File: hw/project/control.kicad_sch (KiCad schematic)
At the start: 46 parts, among them SW1 RESET, SW2 BOOT0, U7 STSPIN32G4, X1 32MHZ 10PF

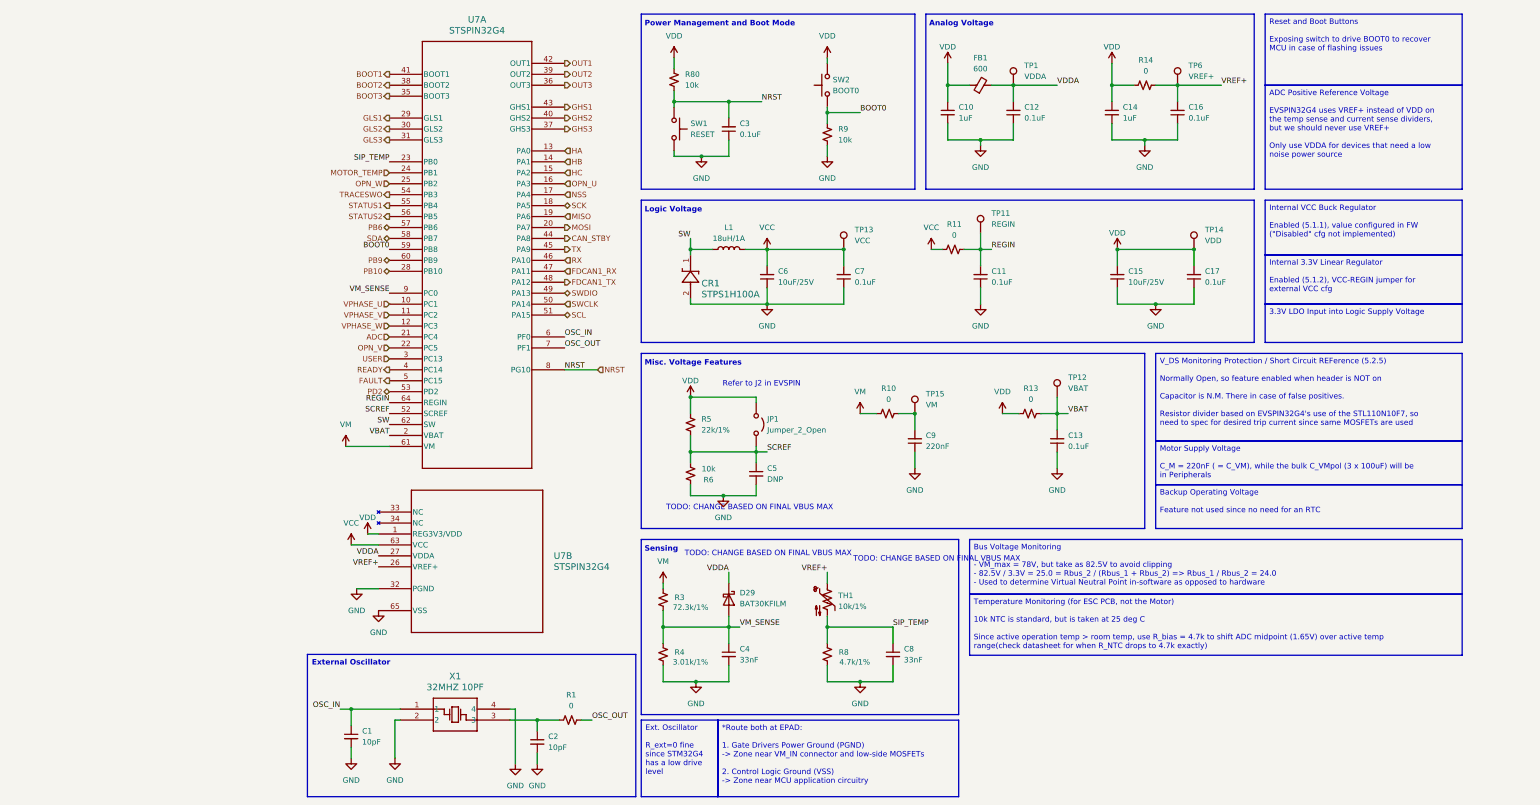
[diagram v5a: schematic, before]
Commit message: Finalize VCC regulator and VDD sections
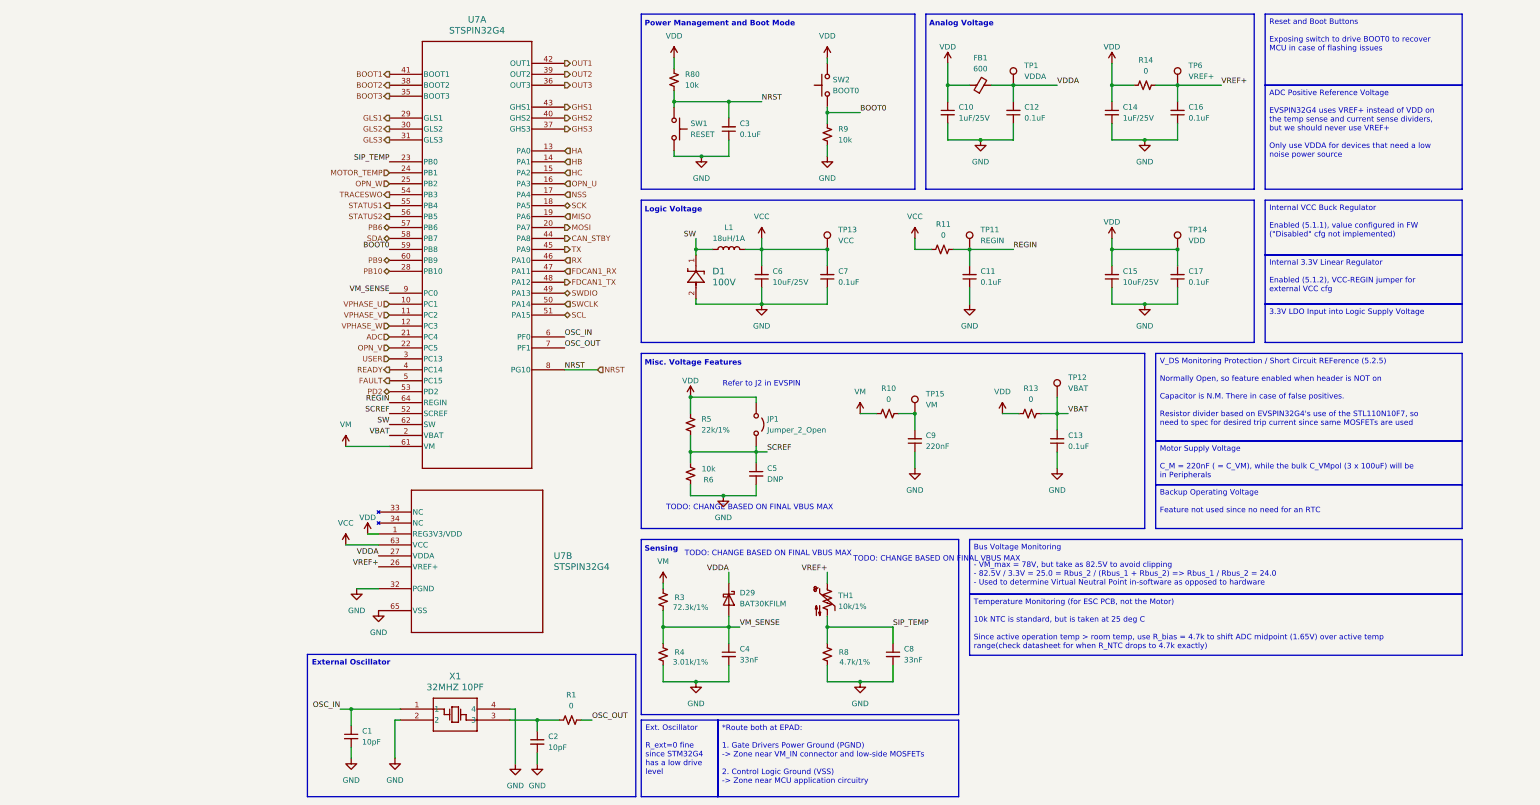
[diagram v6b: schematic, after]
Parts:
- C10, C14: value 1uF -> 1uF/25V
- D1: renamed from CR1; value STPS1H100A -> 100V
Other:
- moved on the sheet: C11, C17, C6, C7, D1, R11, TP11, TP13, TP14

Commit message: Finalize Misc Voltage features
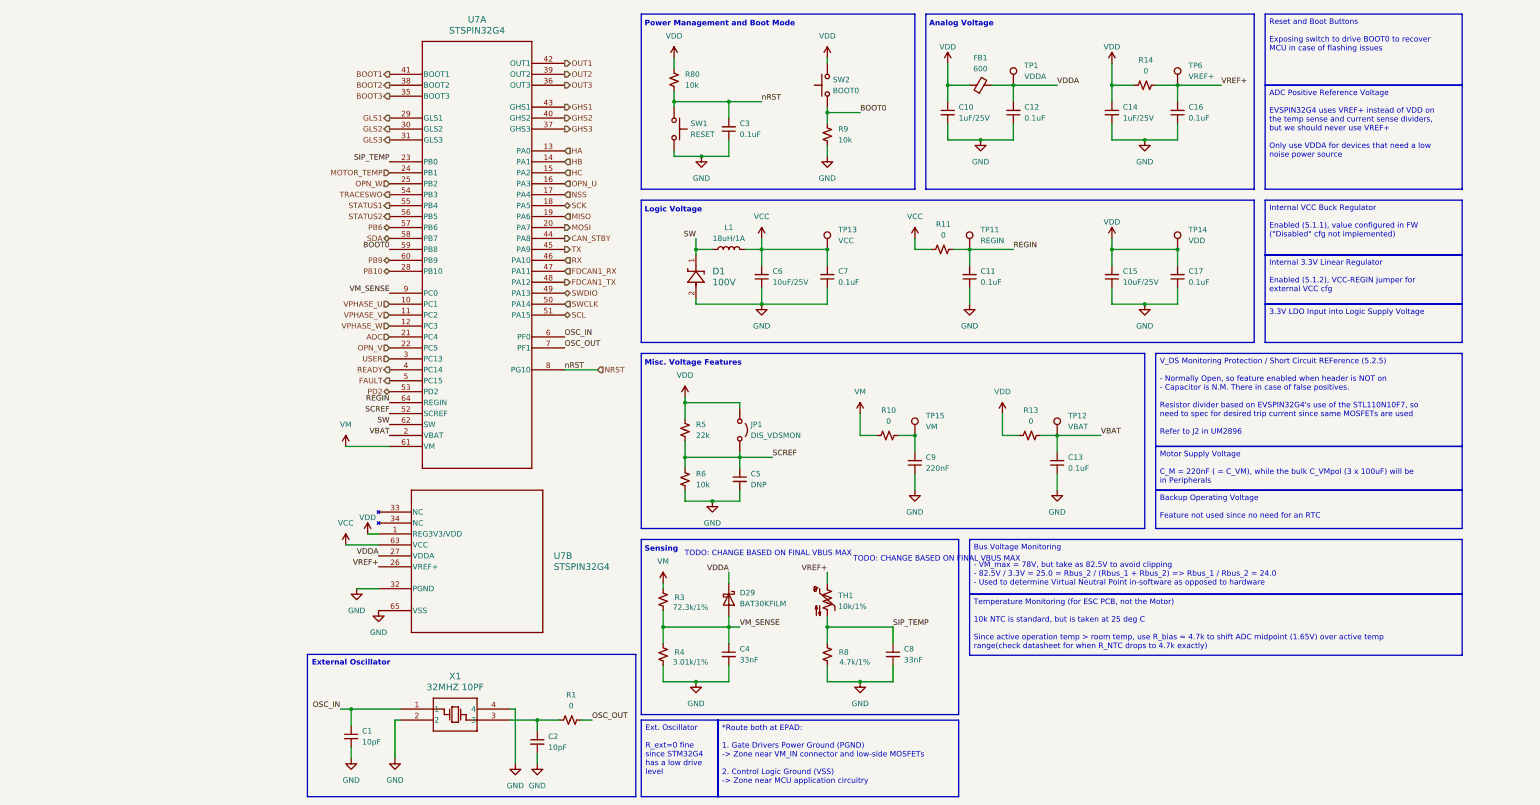
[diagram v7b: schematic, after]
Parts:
- JP1: value Jumper_2_Open -> DIS_VDSMON; footprint (none) -> Connector_PinHeader_2.54mm:PinHeader_1x02_P2.54mm_Vertical
- R5: value 22k/1% -> 22k
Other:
- note removed: "Refer to J2 in EVSPIN"
- moved on the sheet: C13, C5, C9, JP1, R10, R13, R5, R6, TP12, TP15

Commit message: Finished control sheet sensing. Need to work on OSC tomorrow
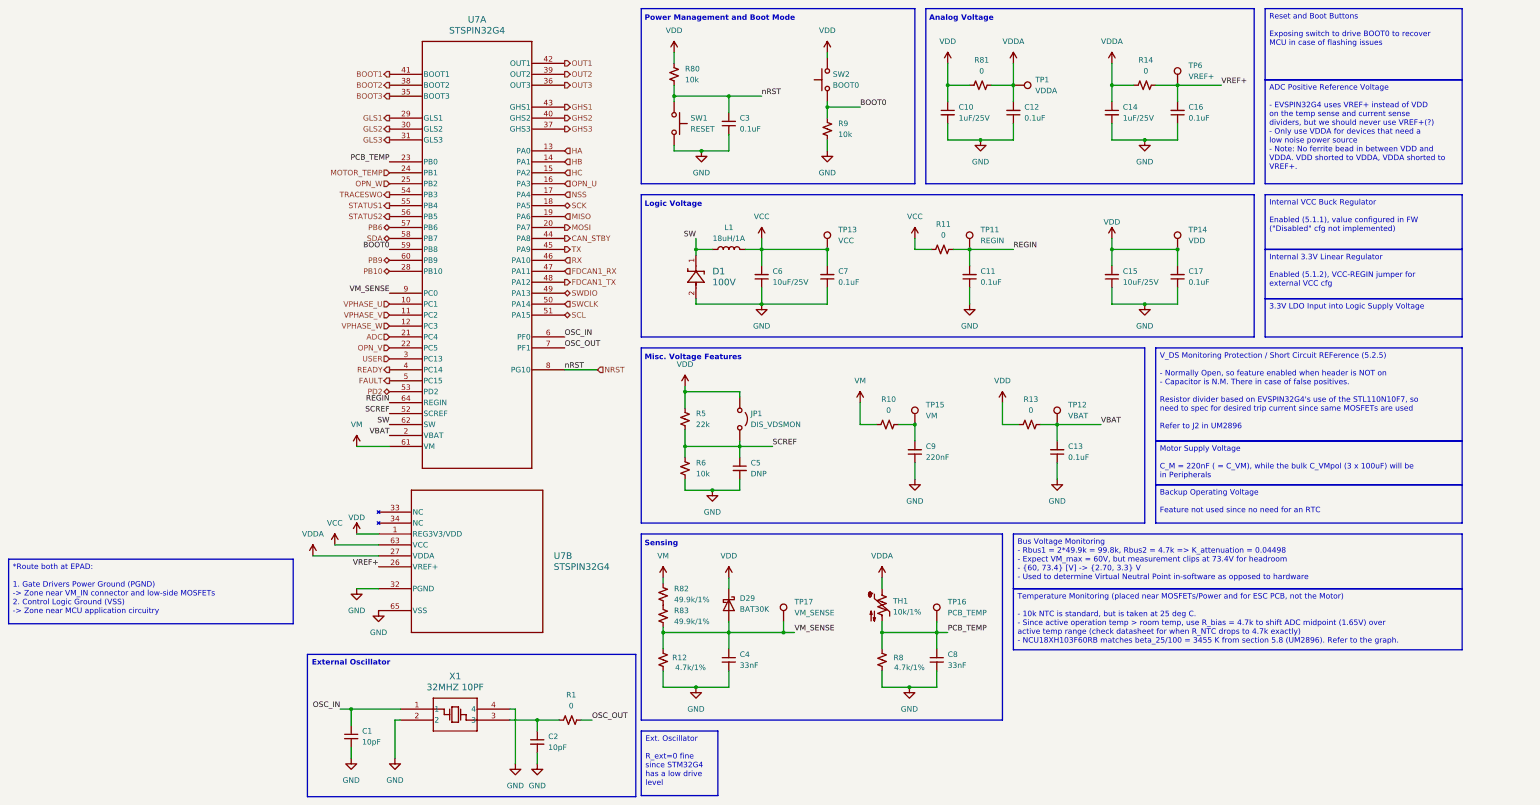
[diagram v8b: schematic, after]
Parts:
- removed FB1: 600, Inductor_SMD:L_0603_1608Metric, symbol Device:FerriteBead_Small
- removed R3: 72.3k/1%, Resistor_SMD:R_0603_1608Metric, symbol Device:R_Small_US
- removed R4: 3.01k/1%, Resistor_SMD:R_0603_1608Metric, symbol Device:R_Small_US
- added R12: 4.7k/1%, Resistor_SMD:R_0603_1608Metric, symbol Device:R_Small_US
- added R81: 0, Resistor_SMD:R_0603_1608Metric, symbol Device:R_Small_US
- added R82, R83: 49.9k/1%, Resistor_SMD:R_0603_1608Metric, symbol Device:R_Small_US
- added TP16: PCB_TEMP, TestPoint:TestPoint_Pad_D1.0mm, symbol Connector:TestPoint
- added TP17: VM_SENSE, TestPoint:TestPoint_Pad_D1.0mm, symbol Connector:TestPoint
- D29: value BAT30KFILM -> BAT30K
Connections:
- net GND: now also R12.2
- net VDD: now also D29.1 (K), R81.1; no longer C14.1, R14.1
- net VDDA: now also C14.1, R14.1, TH1.1, R81.2; no longer D29.1 (K)
- net VM: now also R82.1
- net VM_SENSE: now also R12.1, R83.2, TP17.1
- net VREF+: no longer TH1.1
- net SIP_TEMP renamed PCB_TEMP
- net PCB_TEMP: now also TP16.1
- new net: R82.2, R83.1
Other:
- note removed: "TODO: CHANGE BASED ON FINAL VBUS MAX"
- moved on the sheet: C13, C3, C4, C5, C8, C9, D29, JP1, R10, R13, R5, R6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
